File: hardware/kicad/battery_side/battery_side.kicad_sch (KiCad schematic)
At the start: 41 parts, among them J1 Conn_01x02, J2 RJ45, J3 USB-OTG, J5 UART-DBG, Q1 AO3401A, Q2 AO3400A, U1 TPS62933FDRLR, U2 R-78E12-1.0, U3 SN65HVD3082E

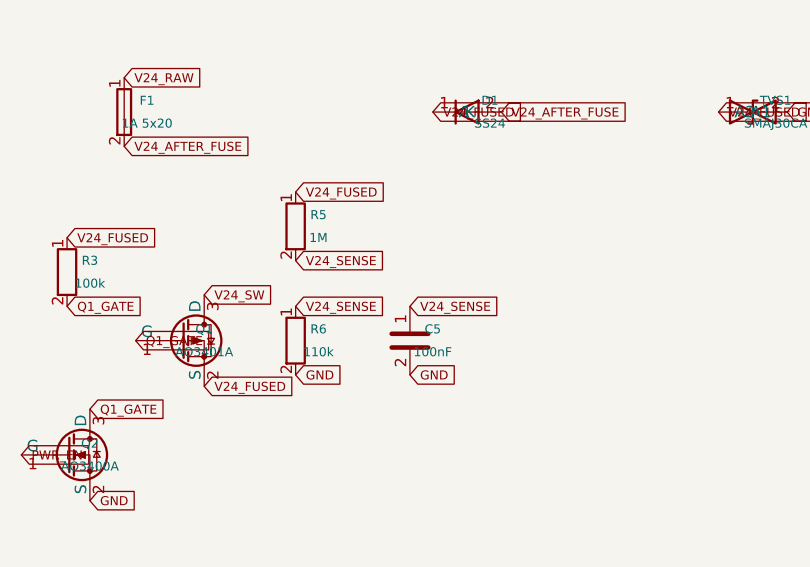
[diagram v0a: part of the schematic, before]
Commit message: hardware: CP-schematic-cleanup iter 22 — Finding 07 (sense divider) fix
R5 + R6 + C5 form the V24_SENSE divider. All three shared the
V24_SENSE net at adjacent pin endpoints (within a 13x13mm box) but
each had its own label — producing the dense V24_SENSE/V24_FUSED
cluster Codex flagged.

Fix — proper schematic semantics: 1 label + 2 wires.
  - Dropped V24_SENSE labels at R5.pin2 and C5.pin1
  - Kept single V24_SENSE label at R6.pin1 (divider midpoint)
  - Added wires:
      R5.pin2 → R6.pin1 (vertical at x=101.6)
      R6.pin1 → C5.pin1 (horizontal at y=59.69)

Three labels of identical text → one label + two visible wires.
This is the schematic style criterion #2 wanted: wires between
adjacent components, labels only where needed.

ERC 0/0 both schematics (topology preserved by single label +
wires being on-grid and pin-aligned).
PCB DRC 0 errors.

Visual check: the sense-divider area now reads cleanly:
  V24_FUSED
    |
   R5 — V24_SENSE — C5
    |                |
   R6              GND
    |
   GND

SEMAPHORE -> codex_turn iter 23.

Co-Authored-By: Claude Opus 4.7 (1M context) <noreply@anthropic.com>
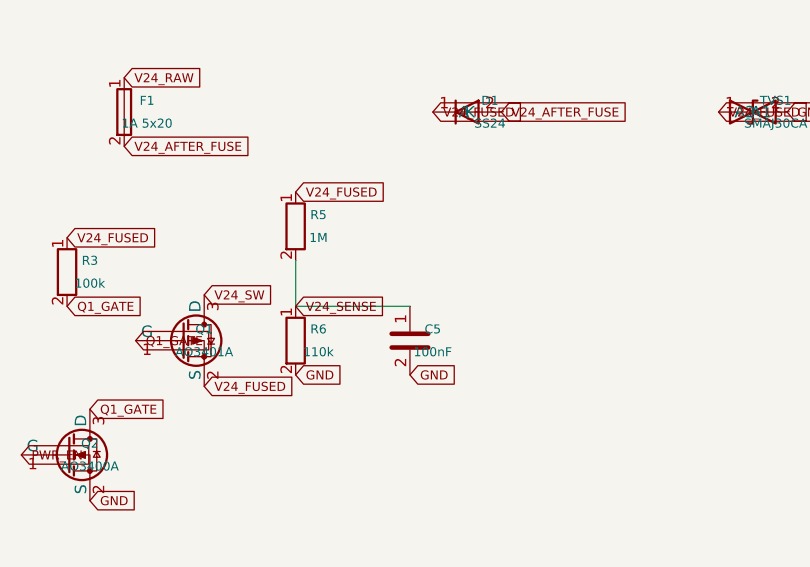
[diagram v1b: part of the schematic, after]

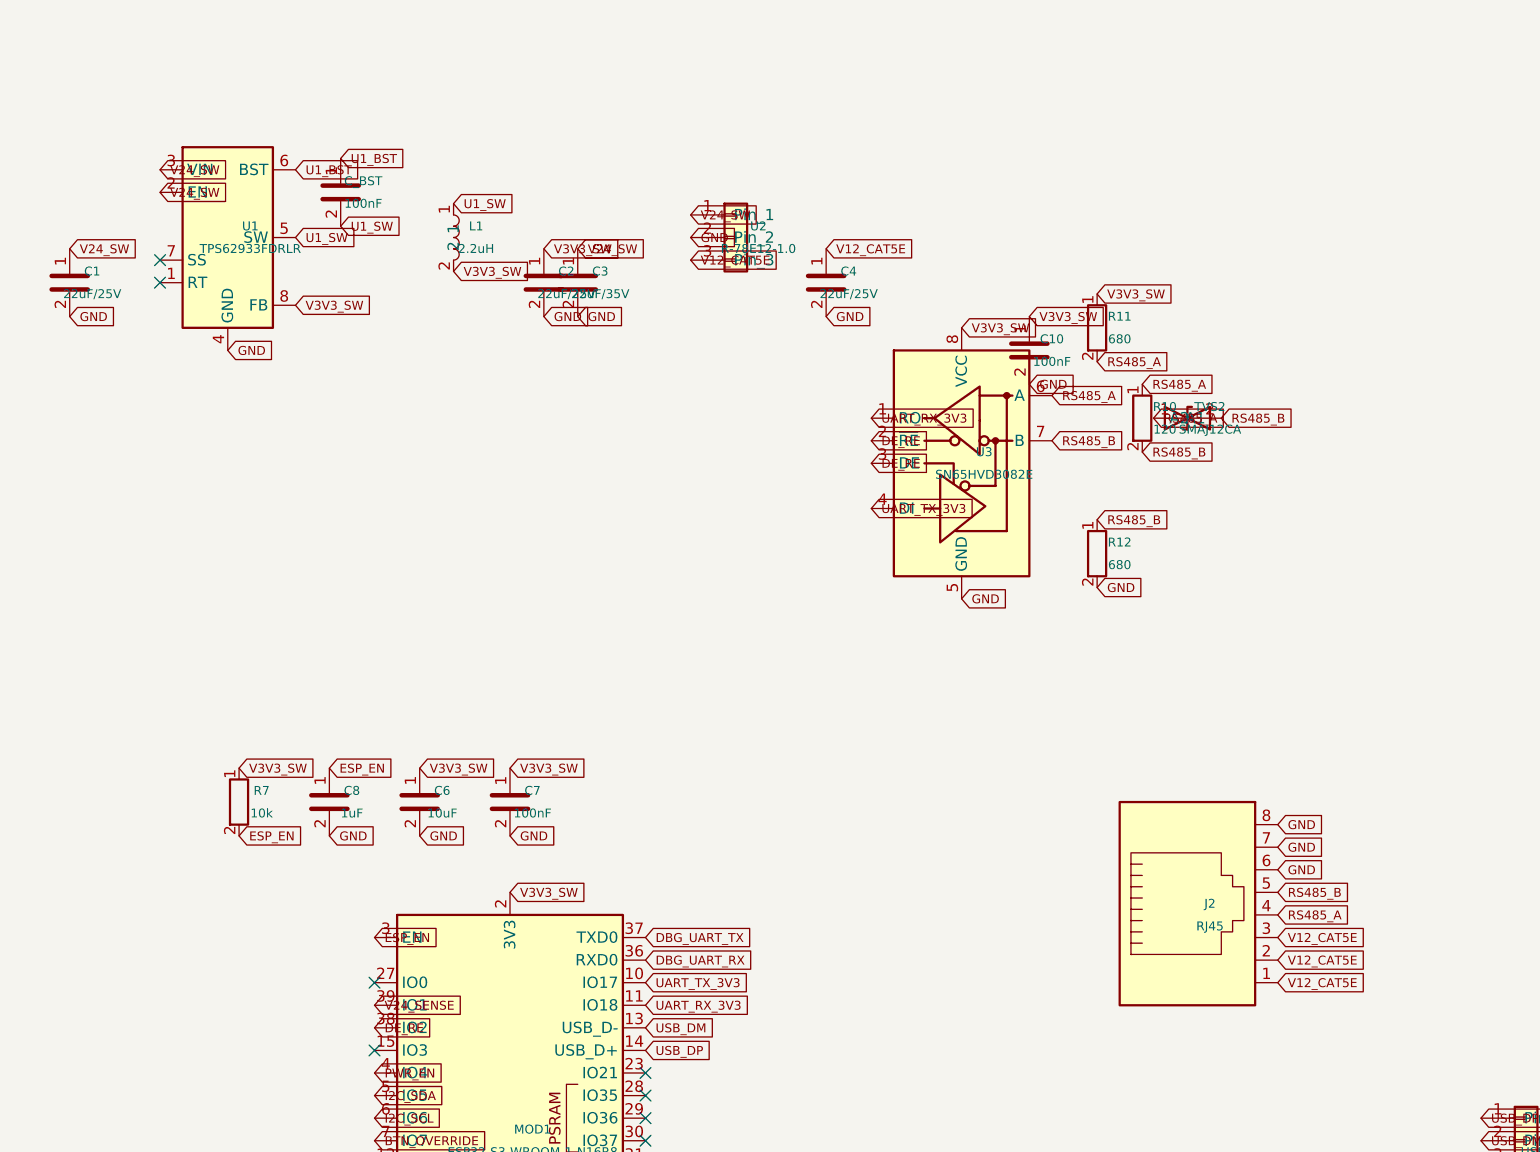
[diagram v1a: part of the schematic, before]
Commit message: hardware: CP-schematic-cleanup iter 24 — 5 more shared-net dedupes
Continuing the Finding 07 pattern. Five more multi-pin same-net
junctions converted to single-label + wire(s):

  Battery-side J2 RJ45: V12_CAT5E (pins 1/2/3) and GND (pins 6/7/8)
                        — 6 labels → 2 + per-pin-pair wires
  Display-side J1 RJ45: same pattern — 6 labels → 2
  Battery-side U1: EN (pin 2) + VIN (pin 3) tied to V24_SW — wire+label
  Battery-side U3: ~RE (pin 2) + DE (pin 3) tied DE_RE — wire+label
  Display-side U2: same DE_RE tie — wire+label

ERC fix: KiCad doesn't auto-connect at mid-wire pin endpoints. A
wire that PASSES THROUGH a third pin's endpoint is treated as
dangling unless either an explicit junction is placed OR the wire
is broken into per-pin-pair segments. Chose segments — cleaner
in the source.

Each RJ45 rail now uses 2 wire segments (pin1↔pin2, pin2↔pin3)
with one label at the middle pin. ERC back to 0/0 both boards.

Audit progress:
  battery_side same-net pairs <10mm: 22 → 14 (−8)
  display_side same-net pairs <10mm: 18 → 11 (−7)
  battery_side wires: 2 → 9
  display_side wires: 0 → 5

PCB DRC stays 0 errors.

SEMAPHORE -> codex_turn iter 25.

Co-Authored-By: Claude Opus 4.7 (1M context) <noreply@anthropic.com>
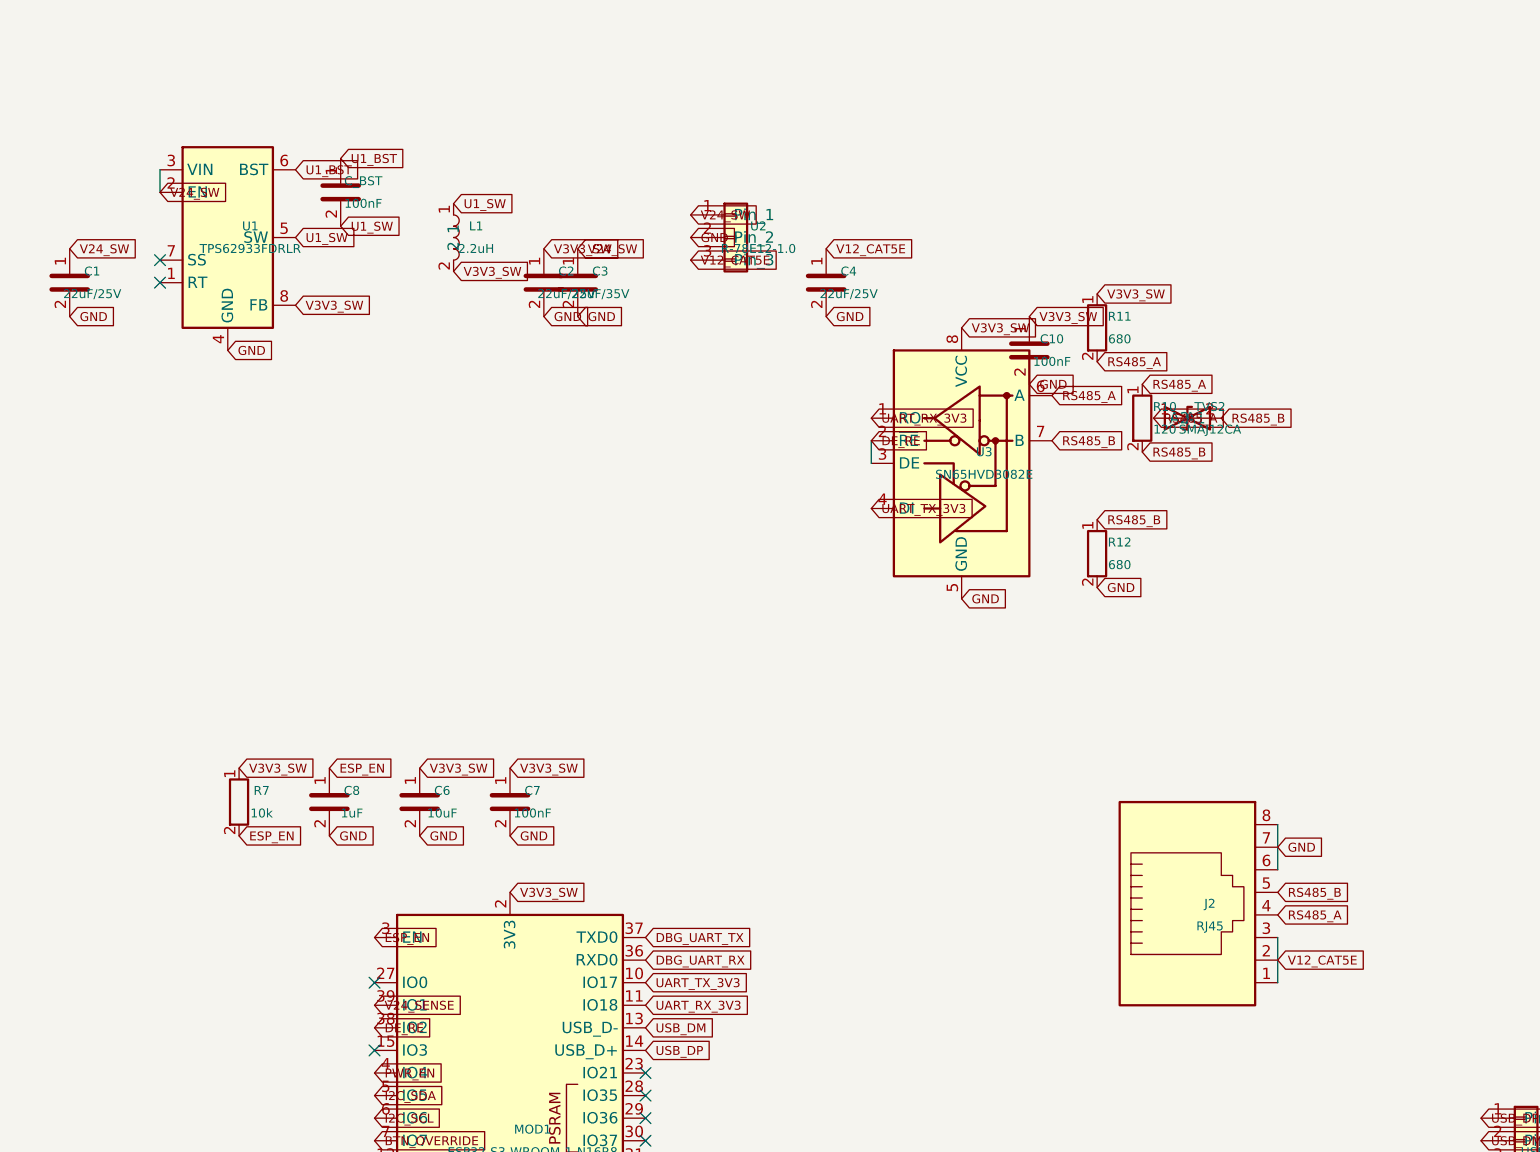
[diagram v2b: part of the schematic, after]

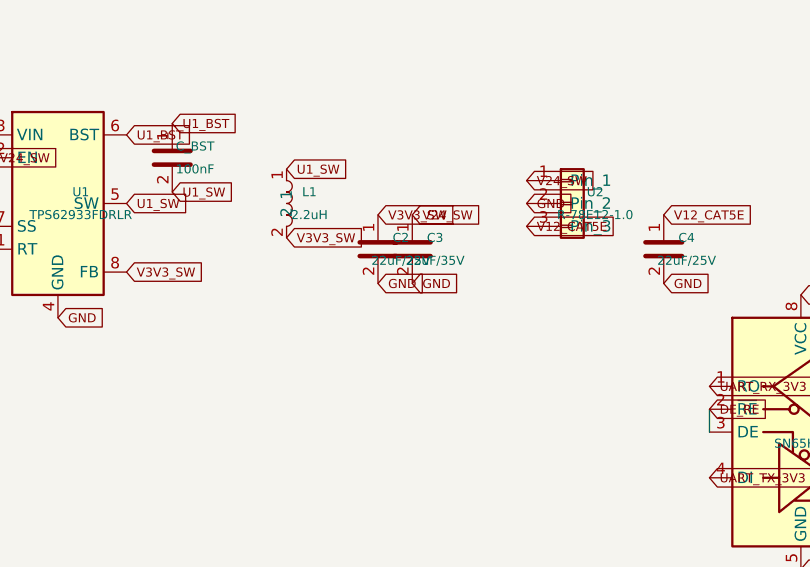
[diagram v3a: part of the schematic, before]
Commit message: hardware: CP-schematic-cleanup iter 28 — C2/C3 GND dedup
Audit found C2 (V3V3 output bulk) and C3 (V12 input bulk) both
labeled GND at the bottom pin, just 3.81mm apart at y=46.99 —
visually adjacent labels of the same net.

Fix: dropped C2's GND label; added a horizontal wire from
C2.pin2 to C3.pin2. C3's GND label defines the shared node.

ERC 0/0 both schematics. PCB DRC 0 errors.

Approaching max_iterations=30. Codex: APPROVE if remaining
clusters are inherent (chip pin density), or flag next offender.

SEMAPHORE -> codex_turn iter 29.

Co-Authored-By: Claude Opus 4.7 (1M context) <noreply@anthropic.com>
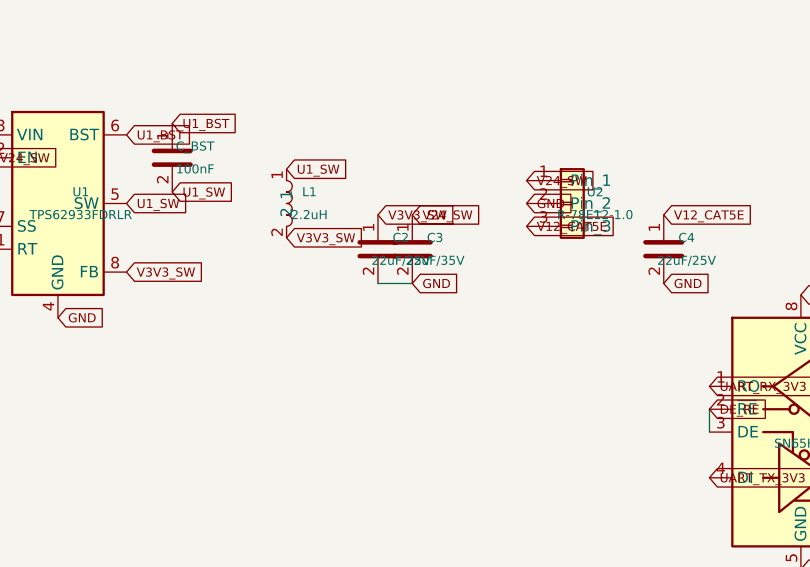
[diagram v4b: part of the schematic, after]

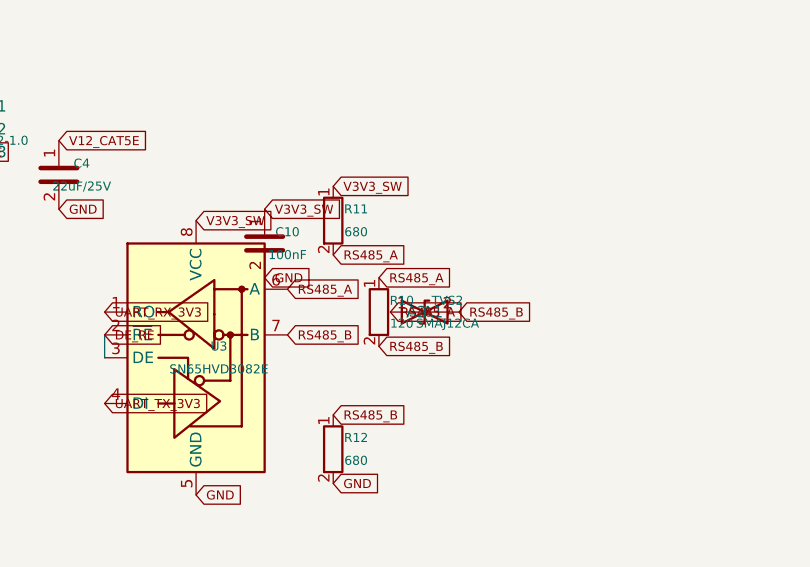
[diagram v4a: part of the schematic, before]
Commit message: hardware: CP-schematic-cleanup iter 30 — RS-485 cluster dedup both boards
User authorized continuing past the iter-30 cap ("forward progress
is what is important"). Bumped max_iterations_per_cp 30→40.

Both RS-485 transceiver areas had 4 RS485_A labels in close
proximity:
  Battery U3: U3.A, R10.pin1, R11.pin2, TVS2.pin1
  Display U2: U2.A, R2.pin1, R3.pin2, TVS2.pin1

Applied wire+single-label dedup with L-shaped wire paths:
  - R10/R2 keeps its RS485_A label
  - R11/R3 label dropped, replaced by wire
  - TVS2 label dropped, replaced by wire
  - U3/U2.A keeps its own label (name connects across schematic)

4 RS485_A labels per cluster → 2 per cluster. 4 labels saved
total, 8 new wires.

Audit progress:
  battery same-net <10mm pairs: 14 → 9 (−5)
  display same-net <10mm pairs: 11 → 6 (−5)
  battery wires: 11 → 14
  display wires: 6 → 10

ERC 0/0 both schematics. PCB DRC 0 errors.

SEMAPHORE -> codex_turn iter 31.

Co-Authored-By: Claude Opus 4.7 (1M context) <noreply@anthropic.com>
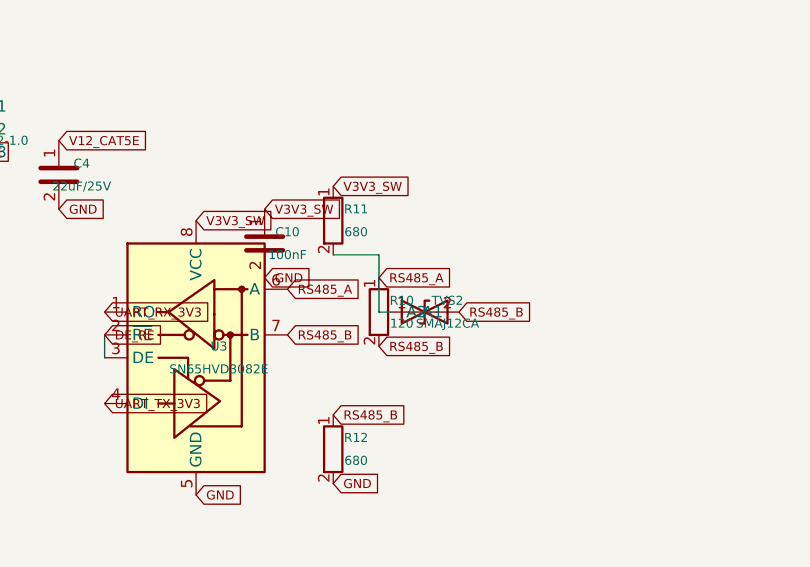
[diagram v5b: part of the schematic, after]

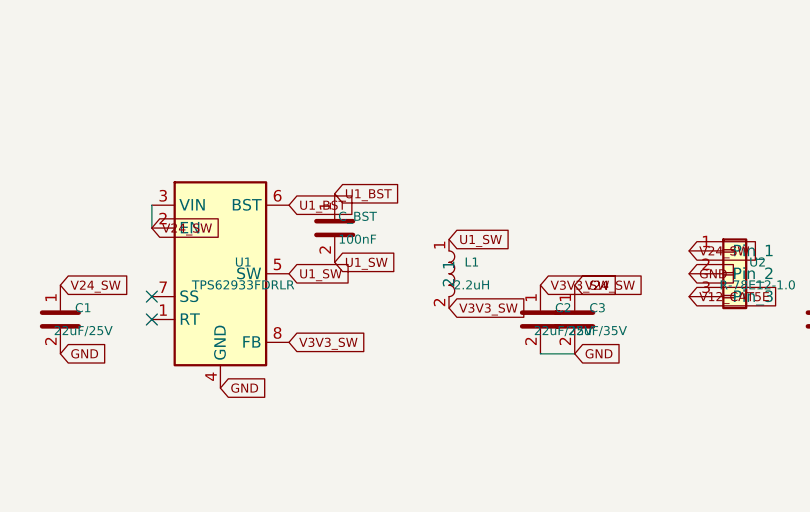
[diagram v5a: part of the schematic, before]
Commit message: hardware: CP-schematic-cleanup iter 32 — Finding 09 (U1 switcher) fix
Battery U1 TPS62933 switcher had U1_BST and U1_SW labels duplicated
~5.24mm apart between U1 pins and adjacent C_BST + L1 pin endpoints.

Fix:
  - Dropped C_BST.pin1 "U1_BST" label → wire to U1.BST
  - Dropped C_BST.pin2 "U1_SW"  label → wire to U1.SW
  - Dropped L1.pin1    "U1_SW"  label → wire to U1.SW

U1 keeps both U1_BST and U1_SW labels (one per net at the chip
pin). C_BST and L1 connections are now explicit via L-shaped
wires.

Audit:
  battery same-net <10mm pairs: 9 → 7 (−2)
  battery wires: 14 → 20 (+6)

ERC 0/0 both schematics. PCB DRC 0 errors.

SEMAPHORE -> codex_turn iter 33.

Co-Authored-By: Claude Opus 4.7 (1M context) <noreply@anthropic.com>
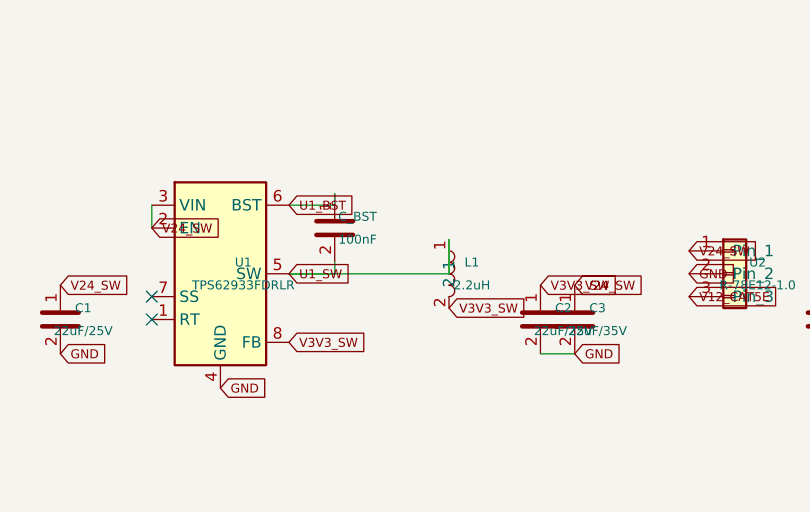
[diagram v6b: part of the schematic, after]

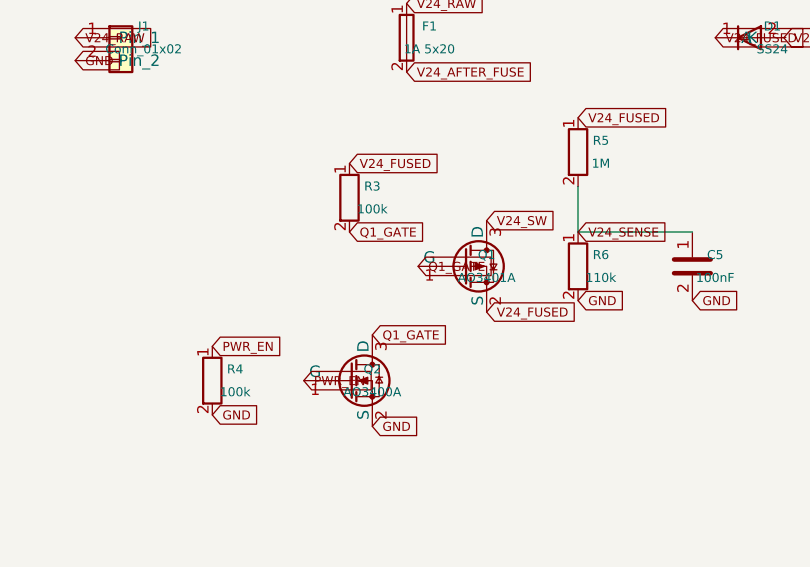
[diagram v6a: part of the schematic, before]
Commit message: hardware: CP-schematic-cleanup iter 34 — Finding 10 (Q1_GATE) fix
Battery hard-cut had Q1_GATE labels at three pin endpoints forming
a tight triangle:
  Q1.G    (83.82, 63.5)
  Q2.D    (78.74, 71.12)
  R3.pin2 (76.2,  59.69)

Fix: Q1 keeps its Q1_GATE label. Q2.D and R3.pin2 labels dropped
and replaced with L-shaped wires connecting to Q1.G:
  Q2.D    → vertical up to (78.74, 63.5) → horizontal right to Q1.G
  R3.pin2 → vertical down to (76.2, 63.5) → horizontal right to Q1.G

Audit:
  battery same-net <10mm pairs: 7 → 5 (−2)
  battery wires: 20 → 24 (+4)

ERC 0/0 both. PCB DRC 0.

SEMAPHORE -> codex_turn iter 35.

Co-Authored-By: Claude Opus 4.7 (1M context) <noreply@anthropic.com>
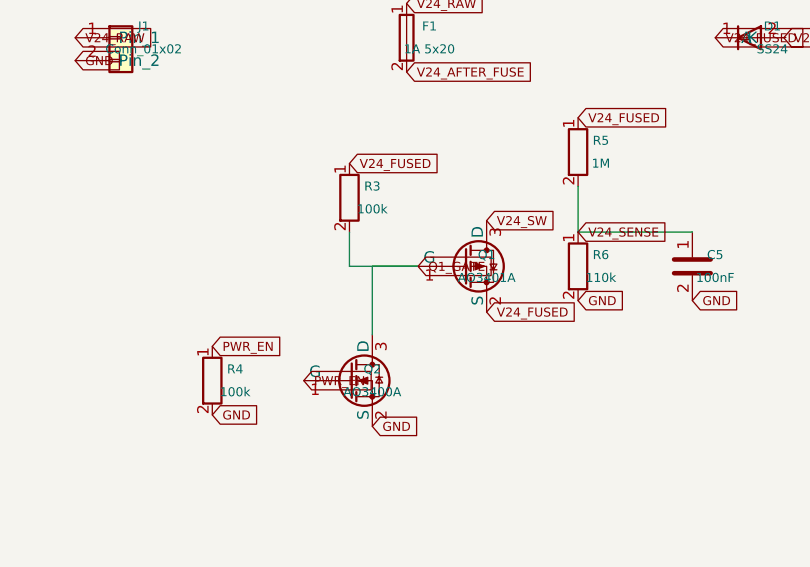
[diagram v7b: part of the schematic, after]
